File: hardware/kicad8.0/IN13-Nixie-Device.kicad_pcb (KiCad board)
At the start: 2 copper layers, 38.1 x 43.1 mm, 35 parts, among them J1 PINHD_1x3_Female, J2 AudioJack3, J3 PINHD_1x4_Male, J4 USB_C_Receptacle_USB2.0_16P, Q2 MMBTA42, T1 Transformer_1P_1S, U1 LM358, U2 STI3508, U3 LD1117S33TR_SOT223, U4 ESP32-C6-MINI-1/U

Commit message: layout progress, kicad proj rename
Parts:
- removed C1: 1uF 16V, Capacitor_SMD:C_0805_2012Metric
- removed C2: 10uF 16V, Capacitor_SMD:C_0805_2012Metric
- C10, C11: footprint Capacitor_SMD:C_0805_2012Metric -> Capacitor_SMD:C_0603_1608Metric
- R3, R6, R7, R8: footprint Resistor_SMD:R_0805_2012Metric -> Resistor_SMD:R_0603_1608Metric
- T1: footprint IN13-Device:EE0504S -> IN13-Nixie-Device:EE0504S
- U3: value LD1117S33TR_SOT223 -> AMS1117-3.3; footprint Package_TO_SOT_THT:TO-220-3_Horizontal_TabDown -> Package_TO_SOT_SMD:SOT-223-3_TabPin2; moved to F.Cu
- moved R6 10.4 mm to (76.5, 68.8), turned to 180 degrees
- moved C10 9.93 mm to (73.3, 68.8), turned to 180 degrees
- moved R10 7.01 mm to (83.3, 59.6), turned to -90 degrees
- moved U3 6.34 mm to (81.1, 49.6), turned to 90 degrees
- moved C5 5.82 mm to (81.5, 56.0), turned to -90 degrees
- moved R9 5.49 mm to (81.4, 59.6), turned to -90 degrees
- moved C9 4.88 mm to (83.4, 43.2), turned to 90 degrees
- moved D2 4.27 mm to (83.7, 56.0)
- moved R7 3.73 mm to (62.6, 70.5), turned to 180 degrees
- moved C11 3.56 mm to (62.6, 74.0), turned to 180 degrees
- moved C6 3.38 mm to (79.2, 56.0), turned to -90 degrees
- moved R1 3.10 mm to (63.2, 49.0), turned to -90 degrees
- moved R8 2.29 mm to (62.6, 72.3), turned to 180 degrees
- moved R3 2.24 mm to (62.6, 68.7)
- moved C3 1.98 mm to (62.1, 53.2)
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
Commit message: starting traces
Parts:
- removed D2: D_Schottky, Diode_SMD:D_0805_2012Metric
- added J5: PINHD_1x4_Male, SharedCustom:Pads_1x4_2.54mm, B.Cu at (71.3, 78.5)
- added R11: 10k, Resistor_SMD:R_0603_1608Metric, F.Cu at (82.0, 74.9)
- added SW1: SW_Push, IN13-Nixie-Device:Mitsumi_SOFSeries_SMD_Button, F.Cu at (57.8, 68.1)
- added SW3: SW_Push, IN13-Nixie-Device:Mitsumi_SOFSeries_SMD_Button, F.Cu at (57.7, 71.9)
- C3: value 220nF 200V -> 0.22u 200V
- J3: footprint Connector_PinHeader_2.54mm:PinHeader_1x04_P2.54mm_Vertical -> SharedCustom:Pads_1x4_2.54mm; moved to B.Cu
- U1: footprint Package_SO:SOIC-8-1EP_3.9x4.9mm_P1.27mm_EP2.41x3.81mm -> Package_SO:SOIC-8_3.9x4.9mm_P1.27mm
- moved J3 30.2 mm to (71.3, 81.0), turned to 180 degrees
- moved R6 6.71 mm to (78.9, 75.1), turned to -90 degrees
- moved C11 6.57 mm to (63.2, 80.6), turned to -90 degrees
- moved C10 6.42 mm to (78.8, 72.1), turned to -90 degrees
- moved R8 5.00 mm to (63.2, 77.2), turned to -90 degrees
- moved R7 3.33 mm to (63.1, 73.8), turned to -90 degrees
- moved R3 1.86 mm to (63.2, 70.5), turned to 90 degrees
- moved C5 1.63 mm to (83.1, 56.0)
- moved C6 1.63 mm to (80.9, 56.0)
- moved C7 1.36 mm to (77.4, 43.0)
- moved C4 1.23 mm to (57.3, 57.1)
- moved U1 1.12 mm to (57.5, 62.4)
- moved J4 1.05 mm to (89.8, 53.2)
- moved R4 1.00 mm to (57.3, 54.7)
- moved R5 0.89 mm to (62.3, 61.8)
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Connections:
- net Net-(U4-EN/CHIP_PU) renamed EN
- C5 pad 1: VIN -> VBUS
- C6 pad 1: VIN -> VBUS
- C7 pad 1: +3V3 -> +3.3V
- C8 pad 1: +3V3 -> +3.3V
- C9 pad 1: +3V3 -> +3.3V
- U3 pad 2: +3V3 -> +3.3V
- U3 pad 3: VIN -> VBUS
- U4 pad 10: unconnected-(U4-MTDI/GPIO5/ADC1_CH5-Pad10) -> TDI
- U4 pad 15: unconnected-(U4-MTCK/GPIO6/ADC1_CH6-Pad15) -> TCK
- U4 pad 16: unconnected-(U4-MTDO/GPIO7-Pad16) -> TDO
- U4 pad 9: unconnected-(U4-MTMS/GPIO4/ADC1_CH4-Pad9) -> TMS
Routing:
- net +3.3V: track 0.00 -> 80.2 mm
- net GND: track 0.02 -> 73.9 mm, vias 0 -> 13
- net HVEN: track 0.00 -> 36.5 mm
- net D-: track 0.00 -> 33.0 mm
- net D+: track 0.00 -> 32.0 mm, vias 0 -> 2
- net Net-(U1A-+): track 0.00 -> 15.2 mm
- net Net-(U2-FB): track 0.00 -> 14.2 mm
- net HV: track 0.00 -> 13.5 mm
- net VBUS: track 0.00 -> 12.5 mm
- net Net-(J4-CC2): track 0.00 -> 10.8 mm, vias 0 -> 2
- net Net-(R2-Pad1): track 0.00 -> 9.83 mm
- net Net-(Q2-E): track 0.00 -> 8.58 mm
- net Net-(T1-AB): track 0.00 -> 8.35 mm
- net Net-(J4-CC1): track 0.00 -> 7.35 mm, vias 0 -> 2
- net Net-(Q2-B): track 0.00 -> 5.12 mm
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- added copper zone on B.Cu, net GND

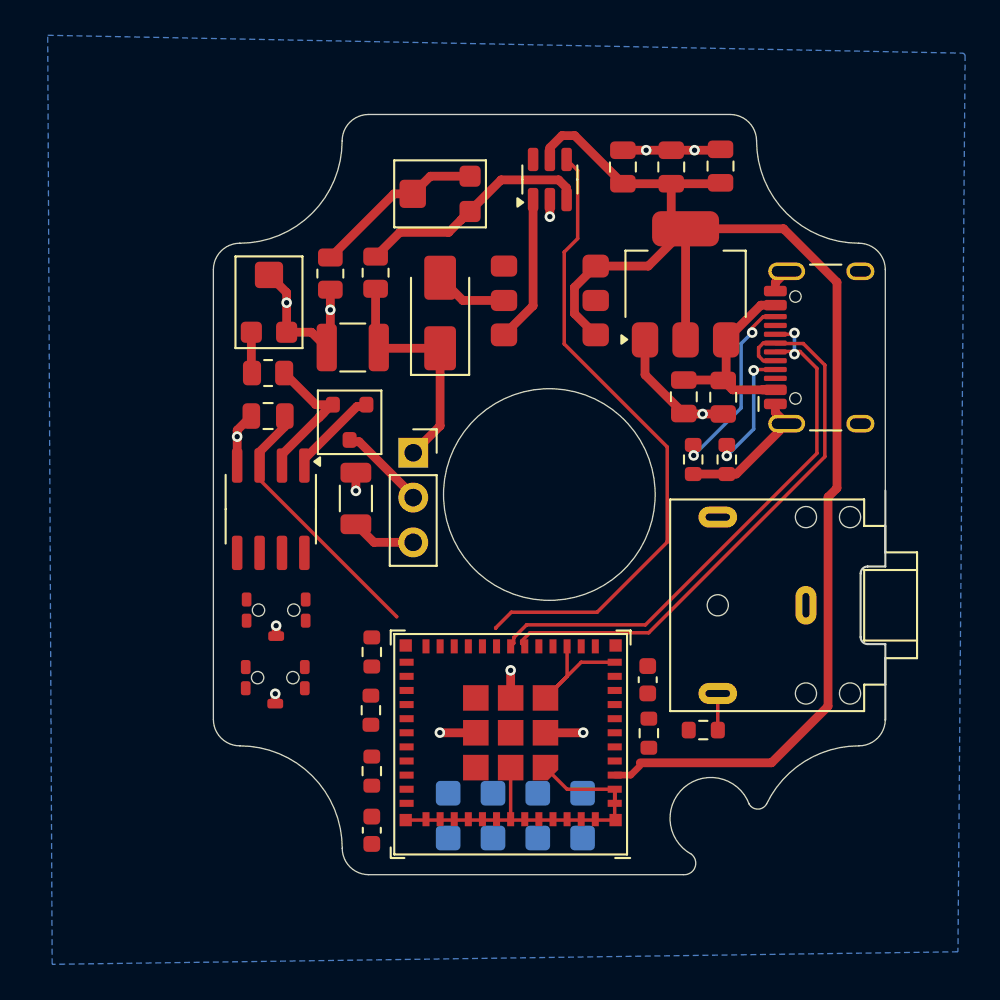
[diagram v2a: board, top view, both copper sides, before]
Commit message: layout passing DRC (except USB conn)
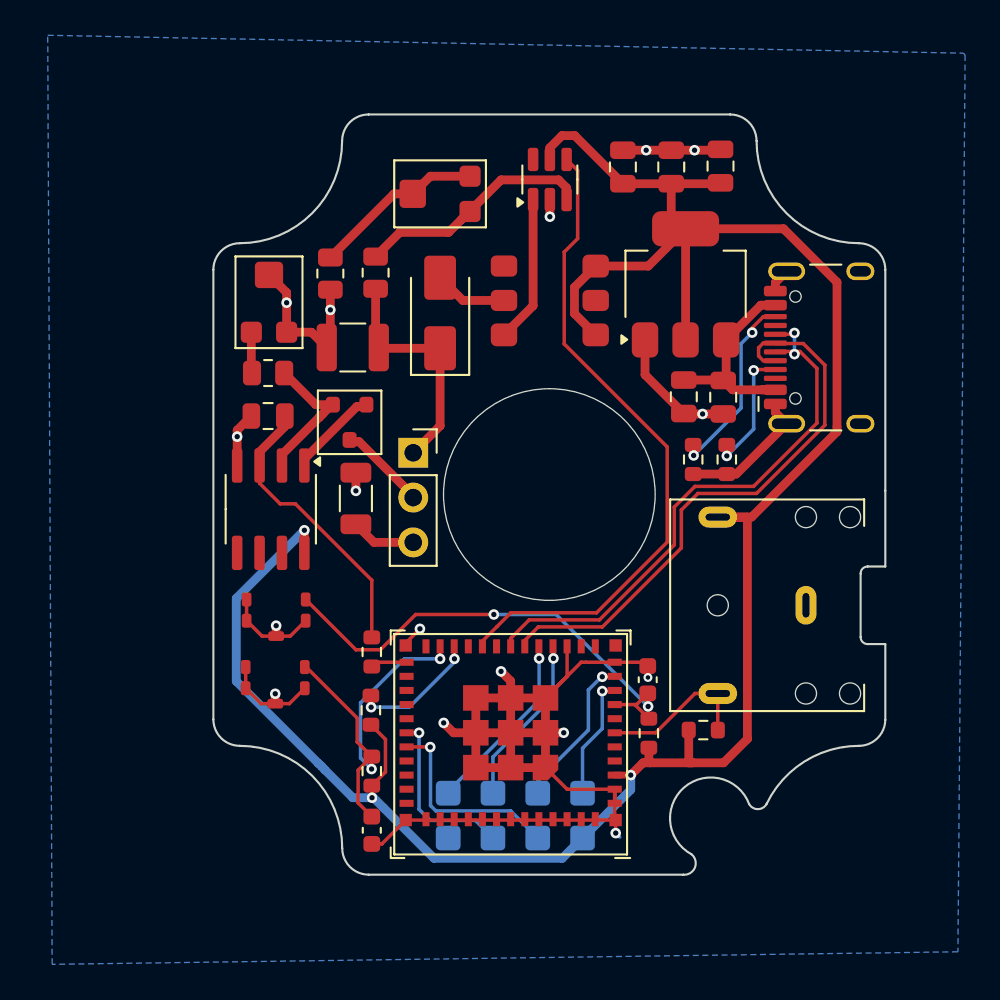
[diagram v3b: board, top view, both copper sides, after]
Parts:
- J2: footprint Connector_Audio:Jack_3.5mm_CUI_SJ1-3523N_Horizontal -> IN13-Nixie-Device:Jack_3.5mm_CUI_SJ1-3523N_Horizontal_NoEdgeSilkscreen
- SW1, SW3: footprint IN13-Nixie-Device:Mitsumi_SOFSeries_SMD_Button -> IN13-Nixie-Device:Mitsumi_SOFSeries_SMD_Button_NoHoles
- turned C10 to 90 degrees
- turned R3 to -90 degrees
- turned R6 to 90 degrees
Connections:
- U4 pad 12: SIGNAL -> unconnected-(U4-GPIO0/ADC1_CH0/XTAL_32K_P-Pad12)
- U4 pad 20: unconnected-(U4-GPIO15-Pad20) -> HVEN
- U4 pad 25: unconnected-(U4-GPIO19-Pad25) -> PWM
- U4 pad 28: PWM -> unconnected-(U4-GPIO22-Pad28)
- U4 pad 29: HVEN -> unconnected-(U4-GPIO23-Pad29)
- U4 pad 6: unconnected-(U4-GPIO3/ADC1_CH3-Pad6) -> SIGNAL
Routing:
- net +3.3V: track 80.2 -> 131.1 mm, vias 0 -> 3
- net GND: track 73.9 -> 112.1 mm, vias 13 -> 16
- net EN: track 0.00 -> 27.6 mm, vias 0 -> 2
- net BOOT: track 0.00 -> 21.6 mm, vias 0 -> 2
- net TX: track 0.00 -> 11.6 mm, vias 0 -> 1
- net TDO: track 0.00 -> 10.5 mm, vias 0 -> 1
- net RX: track 0.00 -> 9.91 mm, vias 0 -> 1
- net TCK: track 0.00 -> 9.75 mm, vias 0 -> 1
- net TDI: track 0.00 -> 8.83 mm, vias 0 -> 1
- net Net-(U4-GPIO8): track 0.00 -> 7.33 mm, vias 0 -> 2
- net TMS: track 0.00 -> 6.94 mm, vias 0 -> 1
- net SIGNAL: track 2.08 -> 8.84 mm
- net PWM: track 0.00 -> 2.07 mm
- net HVEN: track 36.5 -> 37.8 mm
- net Net-(U1A-+): track 15.2 -> 16.3 mm

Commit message: usb line adjust
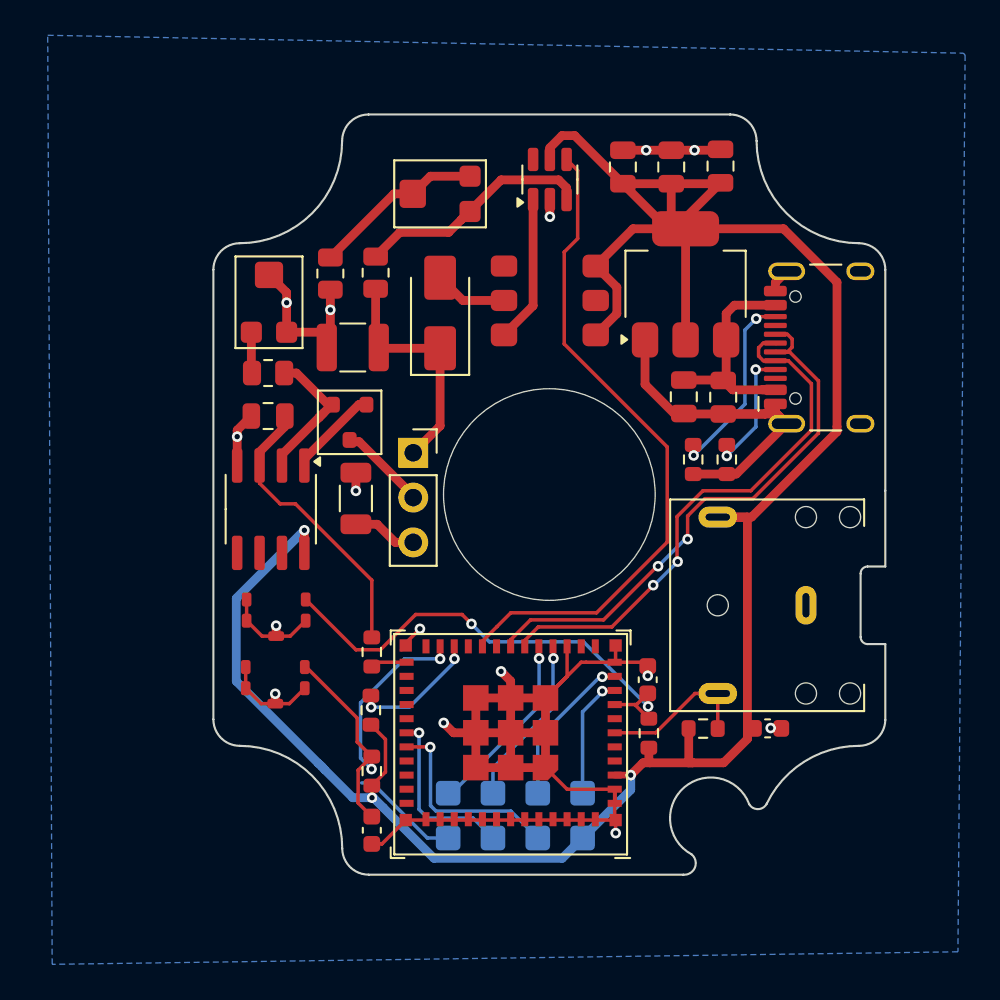
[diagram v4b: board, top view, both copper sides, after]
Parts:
- added C1: 1u, Capacitor_SMD:C_0603_1608Metric, F.Cu at (85.6, 74.8)
- moved R11 0.09 mm to (82.0, 74.8)
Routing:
- net GND: track 112.1 -> 126.7 mm, vias 16 -> 15
- net +3.3V: track 131.1 -> 139.2 mm
- net D-: track 33.0 -> 30.9 mm, vias 0 -> 2
- net VBUS: track 12.5 -> 13.3 mm

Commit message: final board revisions and images
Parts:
- added TP1: TestPoint, TestPoint:TestPoint_Pad_1.0x1.0mm, F.Cu at (61.3, 71.3)
- added TP2: TestPoint, TestPoint:TestPoint_Pad_1.0x1.0mm, F.Cu at (67.4, 67.4)
- added TP3: TestPoint, TestPoint:TestPoint_Pad_1.0x1.0mm, F.Cu at (65.5, 56.3)
- SW1, SW3: footprint IN13-Nixie-Device:Mitsumi_SOFSeries_SMD_Button_NoHoles -> IN13-Nixie-Device:Mitsumi_SOFSeries_SMD_Button
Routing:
- net HVEN: track 37.8 -> 41.4 mm
- net PWM: track 2.07 -> 3.92 mm
- net HV: track 13.5 -> 15.1 mm
- net +3.3V: track 139.2 -> 139.7 mm
